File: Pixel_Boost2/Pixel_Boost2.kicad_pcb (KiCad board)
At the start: 2 copper layers, 27.2 x 14 mm, 10 parts, among them J1 In, J2 Out, U1 MCP1703A-SOT89, U3 74LVC2G14

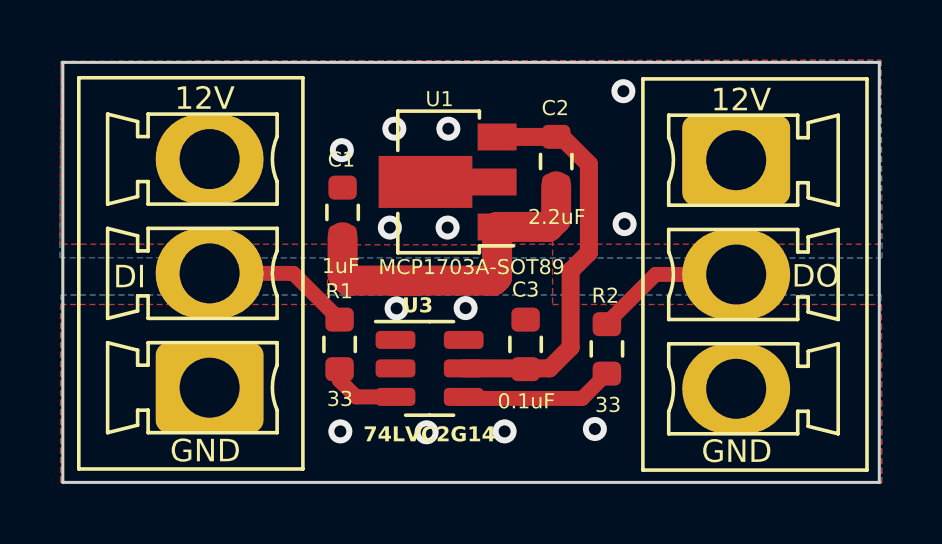
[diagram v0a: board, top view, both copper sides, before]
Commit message: add plug in 3 to 4 adapter
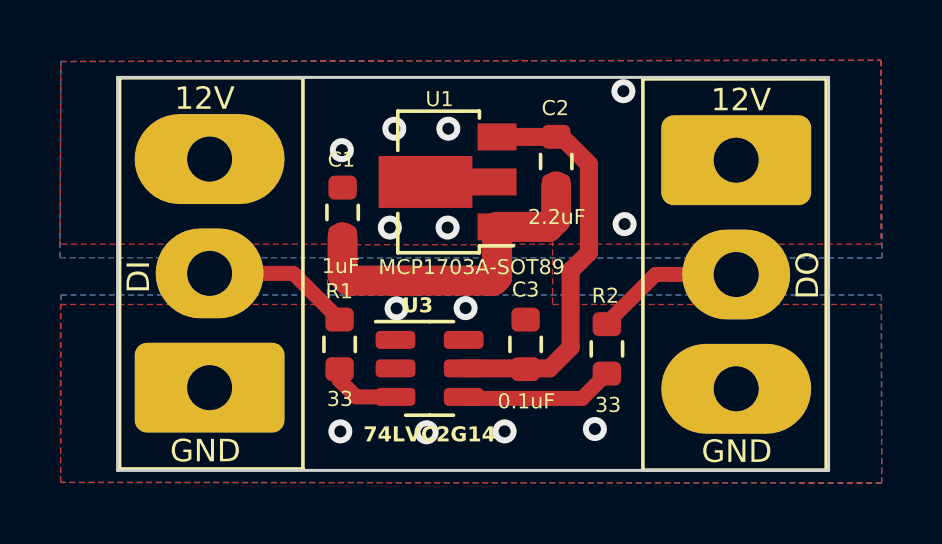
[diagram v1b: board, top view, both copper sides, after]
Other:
- board size 27.2 x 14 mm -> 23.7 x 13.1 mm
